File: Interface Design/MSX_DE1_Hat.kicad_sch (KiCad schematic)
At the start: 25 parts, among them J1 DE1 GPIO, J2 Conn_01x03_Male, J3 Conn_01x03_Male, J4 Conn_01x03_Male, J5 Conn_01x03_Male, J6 Conn_01x03_Male, J7 Conn_01x03_Male, U1 74LVC245A, U2 74LVC245A, U3 74LVC245A, U4 74LVC245A, U5 74LVC245A, U6 4077

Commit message: Renamed the project from MSX IDC Interface to MSX DE1 hat
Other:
- title: MSX IDC Adapter -> MSX DE1 Hat
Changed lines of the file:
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@@
   (paper "A4" portrait)
   (title_block
-    (title "MSX IDC Adapter")
-    (date "2022-12-13")
+    (title "MSX DE1 Hat")
+    (date "2022-12-14")
     (rev "1.1")
     (company "RCC")
     (comment 1 "to 3.3v systems with voltage conversion")
-    (comment 2 "Cartridge for MSX Computers that expose the BUS")
+    (comment 2 "Cartridge for MSX Computers that expose the MSX BUS")
   )
   (junction (at 155.702 155.448) (diameter 0) (color 0 0 0 0)

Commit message: Rev 1.1. Added pull ups for /OE; Changed Pull Ups to 10K; Changed silk screen
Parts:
- added J8: Conn_01x03_Male, Connector_PinHeader_2.54mm:PinHeader_1x03_P2.54mm_Vertical, symbol Connector:Conn_01x03_Male
- added R10, R6, R7, R8, R9: 10K, Resistor_THT:R_Axial_DIN0207_L6.3mm_D2.5mm_P7.62mm_Horizontal, symbol Device:R_Small_US
- R1, R2, R3, R4, R5: value 2.2K -> 10K
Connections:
- net +3.3V: now also J8.1 (Pin_1); no longer C1.2, C2.2, C3.2, C4.2, C5.2, C6.2, R1.1, R2.1, R3.1, R4.1, R5.1, U1.20 (Vcc), U2.20 (Vcc), U3.20 (Vcc), U4.20 (Vcc), U5.20 (Vcc), U6.14 (VDD)
- net +5V: now also J8.3 (Pin_3)
- net at J4.2 (Pin_2), U4.19 (/OE): now also R6.2
- net at J3.2 (Pin_2), U5.19 (/OE): now also R7.2
- net at J7.2 (Pin_2), U1.19 (/OE): now also R10.2
- net at J6.2 (Pin_2), U2.19 (/OE): now also R9.2
- net at J5.2 (Pin_2), U3.19 (/OE): now also R8.2
- new net Vdd: C1.2, C2.2, C3.2, C4.2, C5.2, C6.2, J8.2 (Pin_2), R1.1, R10.1, R2.1, R3.1, R4.1, R5.1, R6.1, R7.1, R8.1, R9.1, U1.20 (Vcc), U2.20 (Vcc), U3.20 (Vcc), U4.20 (Vcc), U5.20 (Vcc), U6.14 (VDD)

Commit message: .
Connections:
- net /WAIT: now also U5.6 (A5); no longer J1.40 (Pin_40)
- net at R4.2, U3.1 (DIR): now also J2.2 (Pin_2), R1.2, R2.2, R3.2, R5.2, U1.1 (DIR), U2.1 (DIR), U4.1 (DIR), U5.1 (DIR)
- net /C_WAIT: now reaches U5.14 (B5)
- net /C_WAIT: now also J1.40 (Pin_40)
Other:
- note removed: "I added some potential workarounds in the schematics to deal with potential errors in the design. If the operatons is not as expected, these workarounds can be tested in the points its available. These workarounds are marked with labels start with "TST?", and descritive texts are added in the locations."
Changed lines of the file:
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@@
   (junction (at 168.656 155.448) (diameter 0) (color 0 0 0 0)
   )
+  (junction (at 75.565 217.043) (diameter 0) (color 0 0 0 0)
+  )
   (junction (at 55.8824 40.511) (diameter 0) (color 0 0 0 0)
   )
+  (junction (at 63.5 177.4106) (diameter 0) (color 0 0 0 0)
+  )
+  (junction (at 70.104 177.4106) (diameter 0) (color 0 0 0 0)
+  )
   (junction (at 94.4597 137.795) (diameter 0) (color 0 0 0 0)
   )
@@
   (junction (at 75.311 58.166) (diameter 0) (color 0 0 0 0)
   )
-  (junction (at 70.116 216.916) (diameter 0) (color 0 0 0 0)
-  )
   (junction (at 112.014 95.123) (diameter 0) (color 0 0 0 0)
   )
@@
   (junction (at 174.498 155.448) (diameter 0) (color 0 0 0 0)
   )
-  (junction (at 70.116 217.043) (diameter 0) (color 0 0 0 0)
+  (junction (at 70.358 137.9834) (diameter 0) (color 0 0 0 0)
   )
   (junction (at 49.53 99.568) (diameter 0) (color 0 0 0 0)
   )
+  (junction (at 70.104 216.916) (diameter 0) (color 0 0 0 0)
+  )
   (junction (at 75.311 97.663) (diameter 0) (color 0 0 0 0)
   )
+  (junction (at 70.358 97.79) (diameter 0) (color 0 0 0 0)
+  )
+  (junction (at 63.368 97.79) (diameter 0) (color 0 0 0 0)
+  )
   (junction (at 55.8824 45.591) (diameter 0) (color 0 0 0 0)
   )
+  (junction (at 73.4493 58.1557) (diameter 0) (color 0 0 0 0)
+  )
   (junction (at 51.054 102.108) (diameter 0) (color 0 0 0 0)
   )
@@
   (junction (at 112.014 135.1588) (diameter 0) (color 0 0 0 0)
   )
+  (junction (at 63.5 58.1557) (diameter 0) (color 0 0 0 0)
+  )
+  (junction (at 70.104 177.292) (diameter 0) (color 0 0 0 0)
+  )
+  (junction (at 63.5 137.9834) (diameter 0) (color 0 0 0 0)
+  )
   (junction (at 94.3839 58.166) (diameter 0) (color 0 0 0 0)
   )
   (junction (at 94.7083 177.292) (diameter 0) (color 0 0 0 0)
   )
+  (junction (at 70.358 137.922) (diameter 0) (color 0 0 0 0)
+  )
   (junction (at 93.8301 97.663) (diameter 0) (color 0 0 0 0)
   )
   (junction (at 174.498 160.528) (diameter 0) (color 0 0 0 0)
   )
-  (junction (at 70.104 216.916) (diameter 0) (color 0 0 0 0)
+  (junction (at 63.368 118.364) (diameter 0) (color 0 0 0 0)
   )
   (junction (at 43.9077 170.688) (diameter 0) (color 0 0 0 0)
@@
   (no_connect (at 32.385 79.248))
   (no_connect (at 32.385 107.188))
-  (wire (pts (xy 70.116 216.916) (xy 70.104 216.916))
-    (stroke (width 0) (type default) (color 0 0 0 0))
-  )
   (wire (pts (xy 43.18 180.848) (xy 43.18 185.928))
     (stroke (width 0) (type default) (color 0 0 0 0))
   )
+  (wire (pts (xy 63.5 216.916) (xy 70.104 216.916))
+    (stroke (width 0) (type default) (color 0 0 0 0))
+  )
+  (wire (pts (xy 63.368 97.79) (xy 63.368 118.364))
+    (stroke (width 0) (type default) (color 0 0 0 0))
+  )
   (wire (pts (xy 49.53 40.4961) (xy 49.53 99.568))
     (stroke (width 0) (type default) (color 0 0 0 0))
   )
+  (wire (pts (xy 63.368 58.1557) (xy 63.368 97.79))
+    (stroke (width 0) (type default) (color 0 0 0 0))
+  )
   (wire (pts (xy 71.1224 42.926) (xy 71.1224 43.051))
     (stroke (width 0) (type default) (color 0 0 0 0))
   )
+  (wire (pts (xy 63.5 216.916) (xy 63.5 177.4106))
+    (stroke (width 0) (type default) (color 0 0 0 0))
+  )
   (wire (pts (xy 168.656 155.448) (xy 174.498 155.448))
     (stroke (width 0) (type default) (color 0 0 0 0))
@@
     (stroke (width 0) (type default) (color 0 0 0 0))
   )
-  (wire (pts (xy 70.116 217.043) (xy 61.214 217.043))
-    (stroke (width 0) (type default) (color 0 0 0 0))
-  )
   (wire (pts (xy 174.498 160.528) (xy 180.34 160.528))
     (stroke (width 0) (type default) (color 0 0 0 0))
@@
     (stroke (width 0) (type default) (color 0 0 0 0))
   )
-  (wire (pts (xy 70.116 217.043) (xy 70.116 216.916))
+  (wire (pts (xy 75.565 216.916) (xy 75.565 217.043))
     (stroke (width 0) (type default) (color 0 0 0 0))
   )
@@
     (stroke (width 0) (type default) (color 0 0 0 0))
   )
+  (wire (pts (xy 70.358 137.9834) (xy 70.358 137.922))
+    (stroke (width 0) (type default) (color 0 0 0 0))
+  )
+  (wire (pts (xy 63.5 137.9834) (xy 70.358 137.9834))
+    (stroke (width 0) (type default) (color 0 0 0 0))
+  )
+  (wire (pts (xy 70.104 216.916) (xy 75.565 216.916))
+    (stroke (width 0) (type default) (color 0 0 0 0))
+  )
   (wire (pts (xy 55.8824 40.4961) (xy 55.8824 40.511))
     (stroke (width 0) (type default) (color 0 0 0 0))
@@
     (stroke (width 0) (type default) (color 0 0 0 0))
   )
-  (wire (pts (xy 56.896 118.364) (xy 61.214 118.364))
+  (wire (pts (xy 56.896 118.364) (xy 63.368 118.364))
     (stroke (width 0) (type default) (color 0 0 0 0))
   )
@@
     (stroke (width 0) (type default) (color 0 0 0 0))
   )
+  (wire (pts (xy 63.5 177.4106) (xy 63.5 137.9834))
+    (stroke (width 0) (type default) (color 0 0 0 0))
+  )
   (wire (pts (xy 92.583 177.292) (xy 94.7083 177.292))
     (stroke (width 0) (type default) (color 0 0 0 0))
@@
     (stroke (width 0) (type default) (color 0 0 0 0))
   )
+  (wire (pts (xy 73.4493 58.1557) (xy 63.5 58.1557))
+    (stroke (width 0) (type default) (color 0 0 0 0))
+  )
   (wire (pts (xy 157.734 52.07) (xy 167.132 52.07))
     (stroke (width 0) (type default) (color 0 0 0 0))
@@
     (stroke (width 0) (type default) (color 0 0 0 0))
   )
+  (wire (pts (xy 63.5 177.4106) (xy 70.104 177.4106))
+    (stroke (width 0) (type default) (color 0 0 0 0))
+  )
+  (wire (pts (xy 63.368 58.1557) (xy 63.5 58.1557))
+    (stroke (width 0) (type default) (color 0 0 0 0))
+  )
   (wire (pts (xy 70.104 177.292) (xy 75.311 177.292))
     (stroke (width 0) (type default) (color 0 0 0 0))
@@
     (stroke (width 0) (type default) (color 0 0 0 0))
   )
+  (wire (pts (xy 63.368 97.79) (xy 70.358 97.79))
+    (stroke (width 0) (type default) (color 0 0 0 0))
+  )
   (wire (pts (xy 94.7083 177.292) (xy 109.3105 177.292))
     (stroke (width 0) (type default) (color 0 0 0 0))
   )
+  (wire (pts (xy 63.5 137.9834) (xy 63.5 118.364))
+    (stroke (width 0) (type default) (color 0 0 0 0))
+  )
   (wire (pts (xy 49.53 99.568) (xy 52.324 99.568))
     (stroke (width 0) (type default) (color 0 0 0 0))
@@
     (stroke (width 0) (type default) (color 0 0 0 0))
   )
-  (wire (pts (xy 75.565 217.043) (xy 70.116 217.043))
-    (stroke (width 0) (type default) (color 0 0 0 0))
-  )
   (wire (pts (xy 144.526 160.528) (xy 149.098 160.528))
     (stroke (width 0) (type default) (color 0 0 0 0))
@@
     (stroke (width 0) (type default) (color 0 0 0 0))
   )
+  (wire (pts (xy 63.368 118.364) (xy 63.5 118.364))
+    (stroke (width 0) (type default) (color 0 0 0 0))
+  )
   (wire (pts (xy 61.214 105.918) (xy 51.054 105.918))
     (stroke (width 0) (type default) (color 0 0 0 0))
@@
     (stroke (width 0) (type default) (color 0 0 0 0))
   )
-  (wire (pts (xy 61.214 118.364) (xy 61.214 217.043))
-    (stroke (width 0) (type default) (color 0 0 0 0))
-  )
   (wire (pts (xy 73.4493 58.1557) (xy 75.311 58.1557))
     (stroke (width 0) (type default) (color 0 0 0 0))
@@
     (stroke (width 0) (type default) (color 0 0 0 0))
   )
-  (text "I added some potential workarounds in the schematics to deal with potential errors in the design.\nIf the operatons is not as expected, these workarounds can be tested in the points its available.\nThese workarounds are marked with labels start with \"TST?\", and descritive texts are added in the\nlocations."
-    (at 13.716 19.304 0)
-    (effects (font (size 1 1)) (justify left bottom))
+  (wire (pts (xy 70.104 177.4106) (xy 70.104 177.292))
+    (stroke (width 0) (type default) (color 0 0 0 0))
   )
   (text "TST4 JP6 Solder Jumper - Closing:\n\n1-2 will make /OE controlled\nby MSX /WR and /RD signals.\n\n2-3 Will ground /OE (logical zero)\nmaking it permantely output enabled.\n\nAddress and Data signals are probably ok\nto have this signal enabled only after \nMSX indicates that the bus is ready (/wr & /rd)"
@@
     )
   )
+  (global_label "{slash}C_WAIT" (shape input) (at 92.456 73.152 0) (fields_autoplaced)
+    (effects (font (size 0.7 0.7)) (justify left))
+    (property "Intersheet References" "${INTERSHEET_REFS}" (id 0) (at 98.0193 73.1083 0)
+      (effects (font (size 0.7 0.7)) (justify left) hide)
+    )
+  )
   (global_label "{slash}C_RD" (shape input) (at 92.456 102.489 0) (fields_autoplaced)
     (effects (font (size 0.7 0.7)) (justify left))
@@
     )
   )
+  (global_label "{slash}WAIT" (shape input) (at 75.184 72.898 180) (fields_autoplaced)
+    (effects (font (size 1.27 1.27)) (justify right))
+    (property "Intersheet References" "${INTERSHEET_REFS}" (id 0) (at 67.328 72.9774 0)
+      (effects (font (size 1.27 1.27)) (justify right) hide)
+    )
+  )
   (global_label "C_D4" (shape input) (at 92.71 229.489 0) (fields_autoplaced)
     (effects (font (size 0.7 0.7)) (justify left))
@@
     )
   )
-  (global_label "{slash}WAIT" (shape input) (at 165.608 127 0) (fields_autoplaced)
-    (effects (font (size 0.7 0.7)) (justify left))
-    (property "Intersheet References" "${INTERSHEET_REFS}" (id 0) (at 169.938 126.9563 0)
-      (effects (font (size 0.7 0.7)) (justify left) hide)
-    )
+  (global_label "{slash}C_WAIT" (shape input) (at 165.608 127 0) (fields_autoplaced)
+    (effects (font (size 0.7 0.7)) (justify left))
+    (property "Intersheet References" "${INTERSHEET_REFS}" (id 0) (at 171.1713 126.9563 0)
+      (effects (font (size 0.7 0.7)) (justify left) hide)
+    )

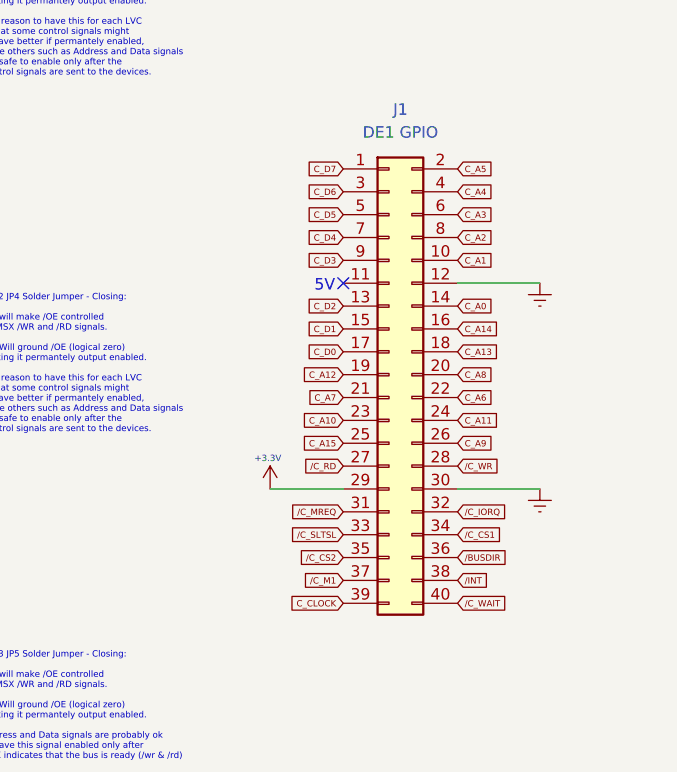
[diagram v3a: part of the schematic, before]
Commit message: Updated PCB Rev 1.1 with IDC connector in right position
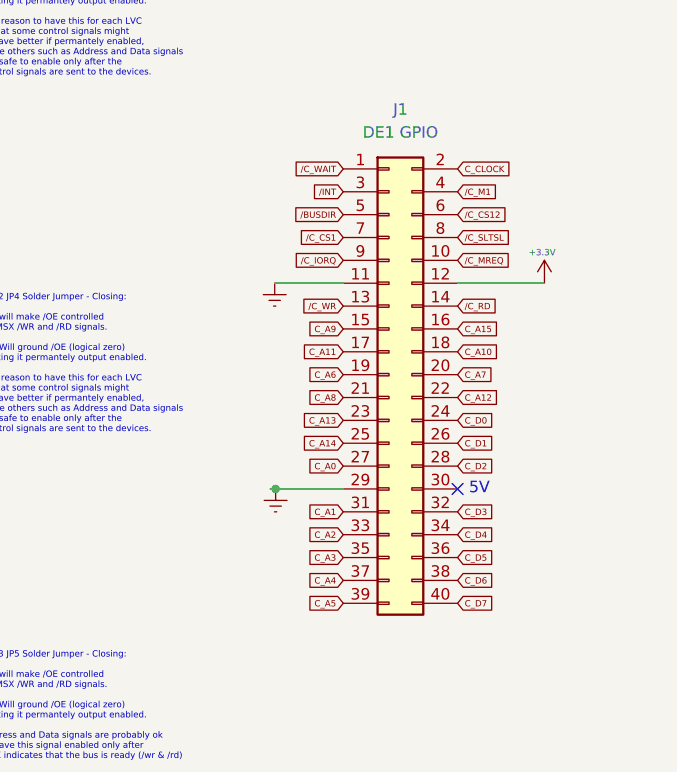
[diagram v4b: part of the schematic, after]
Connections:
- net +3.3V: now also J1.12 (Pin_12); no longer J1.29 (Pin_29)
- net C_A0: now also J1.27 (Pin_27); no longer J1.14 (Pin_14)
- net C_A1: now also J1.31 (Pin_31); no longer J1.10 (Pin_10)
- net C_A10: now also J1.18 (Pin_18); no longer J1.23 (Pin_23)
- net C_A11: now also J1.17 (Pin_17); no longer J1.24 (Pin_24)
- net C_A12: now also J1.22 (Pin_22); no longer J1.19 (Pin_19)
- net C_A13: now also J1.23 (Pin_23); no longer J1.18 (Pin_18)
- net C_A14: now also J1.25 (Pin_25); no longer J1.16 (Pin_16)
- net C_A15: now also J1.16 (Pin_16); no longer J1.25 (Pin_25)
- net C_A2: now also J1.33 (Pin_33); no longer J1.8 (Pin_8)
- net C_A3: now also J1.35 (Pin_35); no longer J1.6 (Pin_6)
- net C_A4: now also J1.37 (Pin_37); no longer J1.4 (Pin_4)
- net C_A5: now also J1.39 (Pin_39); no longer J1.2 (Pin_2)
- net C_A6: now also J1.19 (Pin_19); no longer J1.22 (Pin_22)
- net C_A7: now also J1.20 (Pin_20); no longer J1.21 (Pin_21)
- net C_A8: now also J1.21 (Pin_21); no longer J1.20 (Pin_20)
- net C_A9: now also J1.15 (Pin_15); no longer J1.26 (Pin_26)
- net C_CLOCK: now also J1.2 (Pin_2); no longer J1.39 (Pin_39)
- net C_D0: now also J1.24 (Pin_24); no longer J1.17 (Pin_17)
- net C_D1: now also J1.26 (Pin_26); no longer J1.15 (Pin_15)
- net C_D2: now also J1.28 (Pin_28); no longer J1.13 (Pin_13)
- net C_D3: now also J1.32 (Pin_32); no longer J1.9 (Pin_9)
- net C_D4: now also J1.34 (Pin_34); no longer J1.7 (Pin_7)
- net C_D5: now also J1.36 (Pin_36); no longer J1.5 (Pin_5)
- net C_D6: now also J1.38 (Pin_38); no longer J1.3 (Pin_3)
- net C_D7: now also J1.40 (Pin_40); no longer J1.1 (Pin_1)
- net GNDREF: now also J1.11 (Pin_11), J1.29 (Pin_29); no longer J1.12 (Pin_12), J1.30 (Pin_30)
- net /BUSDIR: now also J1.5 (Pin_5); no longer J1.36 (Pin_36)
- net /C_CS1: now also J1.7 (Pin_7); no longer J1.34 (Pin_34)
- net /C_CS12: now also J1.6 (Pin_6)
- net /C_CS2: no longer J1.35 (Pin_35)
- net /C_IORQ: now also J1.9 (Pin_9); no longer J1.32 (Pin_32)
- net /C_M1: now also J1.4 (Pin_4); no longer J1.37 (Pin_37)
- net /C_MREQ: now also J1.10 (Pin_10); no longer J1.31 (Pin_31)
- net /C_RD: now also J1.14 (Pin_14); no longer J1.27 (Pin_27)
- net /C_SLTSL: now also J1.8 (Pin_8); no longer J1.33 (Pin_33)
- net /C_WAIT: now also J1.1 (Pin_1); no longer J1.40 (Pin_40)
- net /C_WR: now also J1.13 (Pin_13); no longer J1.28 (Pin_28)
- net /INT: now also J1.3 (Pin_3); no longer J1.38 (Pin_38)
